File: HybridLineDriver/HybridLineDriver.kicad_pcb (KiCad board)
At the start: 2 copper layers, 100 x 100 mm, 34 parts, among them J1 XLR3, J2 Conn_01x03, J3 Conn_01x02, U1 OPA1679

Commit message: pcb cleanup
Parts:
- moved C6 2.67 mm to (113.0, 93.3), turned to -90 degrees
- moved C2 1.91 mm to (118.1, 101.6), turned to -90 degrees
- moved R18 1.80 mm to (128.3, 96.5)
- moved R3 1.53 mm to (109.2, 101.6), turned to 90 degrees
- moved R15 1.14 mm to (91.4, 100.3)
- moved R20 1.14 mm to (94.0, 100.3)
- moved R16 1.02 mm to (88.9, 97.4)
- moved R4 0.94 mm to (102.9, 116.2)
- moved R9 0.92 mm to (101.6, 120.0)
- moved C3 0.92 mm to (101.6, 122.6)
- moved R13 0.77 mm to (87.0, 106.3)
- moved C1 0.77 mm to (105.4, 109.2)
- moved RV1 0.76 mm to (97.5, 93.3)
- moved J3 0.64 mm to (134.6, 120.7), turned to 180 degrees
- moved R6 0.57 mm to (125.1, 99.7)
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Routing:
- net Net-(C2-Pad1): track 29.6 -> 34.5 mm
- net Net-(C2-Pad2): track 16.5 -> 20.3 mm
- net Net-(C6-Pad1): track 37.2 -> 40.3 mm
- net GND: track 14.3 -> 16.2 mm
- net Net-(R16-Pad2): track 8.49 -> 9.82 mm
- net Net-(U1B--): track 9.86 -> 11.0 mm
- net Net-(C6-Pad2): track 21.5 -> 22.6 mm
- net Net-(C5-Pad2): track 19.2 -> 20.2 mm
- net Net-(C3-Pad1): track 27.1 -> 28.1 mm
- net Net-(R7-Pad1): track 3.42 -> 4.29 mm
- net Net-(C4-Pad2): track 12.8 -> 11.9 mm
- net +15V: track 44.8 -> 44.0 mm
- net Net-(U1D--): track 14.6 -> 13.9 mm
- net Net-(U1C-+): track 10.6 -> 11.3 mm
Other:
- board size 100 x 100 mm -> 100 x 105 mm

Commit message: update pcb
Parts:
- moved RV1 4.38 mm to (93.3, 94.6)
- moved R3 4.02 mm to (108.0, 105.4)
- moved C3 3.42 mm to (100.3, 119.4), turned to 90 degrees
- moved C4 3.18 mm to (88.3, 106.7), turned to -90 degrees
- moved R4 2.62 mm to (105.4, 116.8)
- moved R9 1.42 mm to (102.9, 119.4), turned to 90 degrees
- moved R20 1.42 mm to (93.3, 101.6)
- moved R11 1.42 mm to (90.8, 123.2)
- moved R15 1.42 mm to (90.8, 101.6)
- moved R19 1.42 mm to (88.3, 123.2)
- moved R13 1.33 mm to (85.7, 106.7)
- moved R12 1.27 mm to (85.7, 113.7)
- moved R14 1.27 mm to (88.3, 116.8)
- moved R2 1.27 mm to (110.5, 105.4), turned to 90 degrees
- moved R16 1.20 mm to (88.3, 98.4)
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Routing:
- net Net-(C1-Pad2): track 15.4 -> 11.1 mm
- net Net-(C3-Pad1): track 28.1 -> 32.2 mm
- net Net-(U1D--): track 13.9 -> 17.8 mm
- net Net-(C4-Pad2): track 11.9 -> 8.02 mm
- net Net-(R16-Pad2): track 9.82 -> 6.05 mm
- net Net-(U1C--): track 12.7 -> 15.5 mm
- net Net-(U1B--): track 11.0 -> 8.93 mm
- net Net-(U1A--): track 8.17 -> 10.1 mm
- net Net-(C5-Pad2): track 20.2 -> 21.6 mm
- net Net-(U1A-+): track 6.64 -> 7.80 mm
- net Net-(R7-Pad1): track 4.29 -> 5.42 mm
- net Net-(C2-Pad1): track 34.5 -> 33.5 mm
- net Net-(U1D-+): track 11.6 -> 10.6 mm
- net GND: track 16.2 -> 15.5 mm
- net Net-(R2-Pad1): track 22.5 -> 21.9 mm

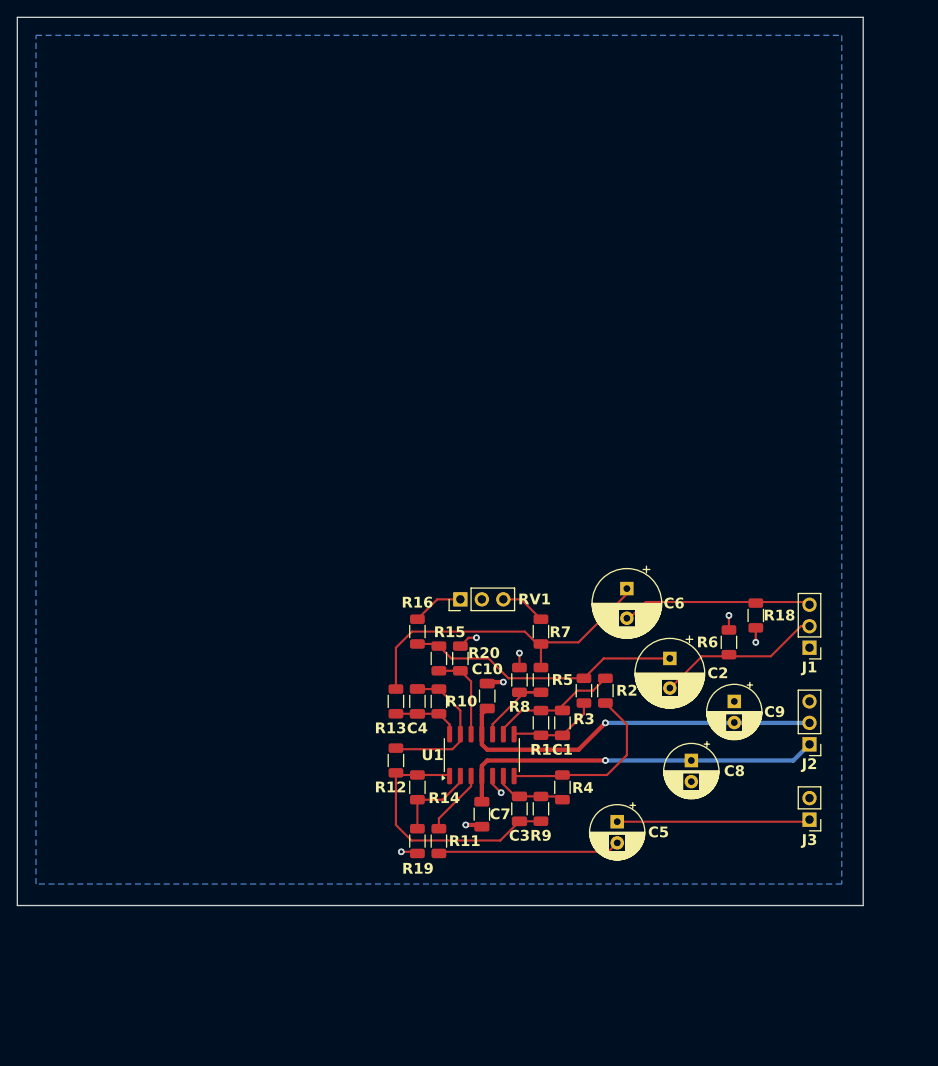
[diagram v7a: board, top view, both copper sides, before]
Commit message: added TLA Input
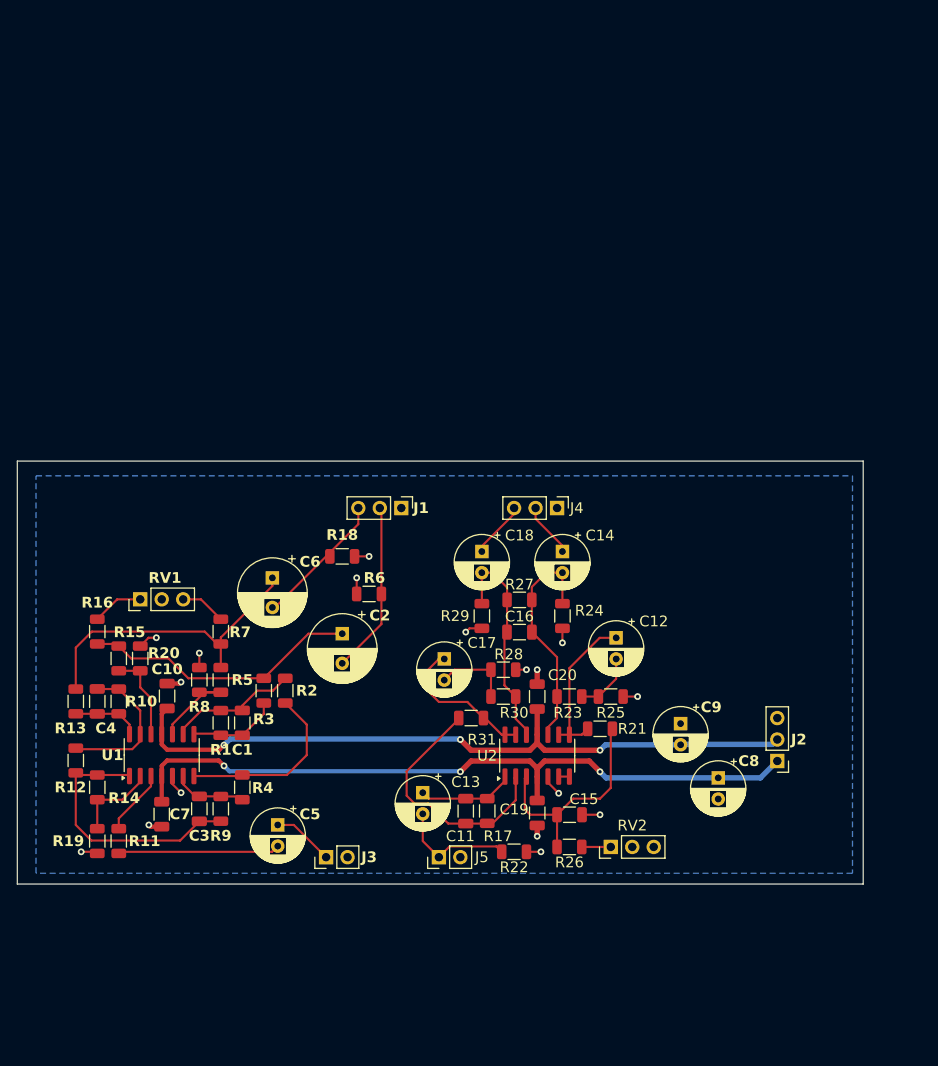
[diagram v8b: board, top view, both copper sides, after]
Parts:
- added C11: 22p, Capacitor_SMD:C_1206_3216Metric, F.Cu at (94.0, 119.6)
- added C12: 22u, Capacitor_THT:CP_Radial_D6.3mm_P2.50mm, F.Cu at (111.8, 99.2)
- added C13: 100u, Capacitor_THT:CP_Radial_D6.3mm_P2.50mm, F.Cu at (88.9, 117.5)
- added C14: 10u, Capacitor_THT:CP_Radial_D6.3mm_P2.50mm, F.Cu at (105.4, 89.0)
- added C15: 22p, Capacitor_SMD:C_1206_3216Metric, F.Cu at (106.2, 120.1)
- added C16: 220p, Capacitor_SMD:C_1206_3216Metric, F.Cu at (100.3, 98.5)
- added C17: 22u, Capacitor_THT:CP_Radial_D6.3mm_P2.50mm, F.Cu at (91.4, 101.7)
- added C18: 10u, Capacitor_THT:CP_Radial_D6.3mm_P2.50mm, F.Cu at (95.9, 89.0)
- added C19: 100n, Capacitor_SMD:C_1206_3216Metric, F.Cu at (102.4, 119.9)
- added C20: 100n, Capacitor_SMD:C_1206_3216Metric, F.Cu at (102.4, 106.1)
- added J4: XLR3, Connector_PinHeader_2.54mm:PinHeader_1x03_P2.54mm_Vertical, F.Cu at (104.8, 83.8)
- added J5: Conn_01x02, Connector_PinHeader_2.54mm:PinHeader_1x02_P2.54mm_Vertical, F.Cu at (90.8, 125.1)
- added R17: 2k, Resistor_SMD:R_1206_3216Metric, F.Cu at (96.5, 119.6)
- added R21: 2k7, Resistor_SMD:R_1206_3216Metric, F.Cu at (109.9, 109.9)
- added R22: 100k, Resistor_SMD:R_1206_3216Metric, F.Cu at (99.7, 124.5)
- added R23: 47k, Resistor_SMD:R_1206_3216Metric, F.Cu at (106.2, 106.1)
- added R24: 10M, Resistor_SMD:R_1206_3216Metric, F.Cu at (105.4, 96.6)
- added R25: 10k, Resistor_SMD:R_1206_3216Metric, F.Cu at (111.1, 106.1)
- added R26: 1k8, Resistor_SMD:R_1206_3216Metric, F.Cu at (106.2, 123.9)
- added R27: 22k, Resistor_SMD:R_1206_3216Metric, F.Cu at (100.3, 94.7)
- added R28: 10k, Resistor_SMD:R_1206_3216Metric, F.Cu at (98.4, 102.9)
- added R29: 10M, Resistor_SMD:R_1206_3216Metric, F.Cu at (95.9, 96.6)
- added R30: 47k, Resistor_SMD:R_1206_3216Metric, F.Cu at (98.4, 106.1)
- added R31: 2k7, Resistor_SMD:R_1206_3216Metric, F.Cu at (94.6, 108.6)
- added RV2: 500R, Connector_PinHeader_2.54mm:PinHeader_1x03_P2.54mm_Vertical, F.Cu at (111.1, 123.9)
- added U2: OPA1679, Package_SO:SOIC-14_3.9x8.7mm_P1.27mm, F.Cu at (102.4, 113.1)
- moved J3 57.3 mm to (77.5, 125.1), turned to 90 degrees
- moved J1 51.0 mm to (86.4, 83.8), turned to -90 degrees
- moved R18 49.4 mm to (79.4, 89.5), turned to 180 degrees
- moved R6 42.9 mm to (82.5, 94.0), turned to 0 degrees
- moved C6 41.9 mm to (71.1, 92.1)
- moved C5 40.1 mm to (71.8, 121.3)
- moved C2 38.8 mm to (79.4, 98.7)
- moved C1 37.8 mm to (67.6, 109.2)
- moved C4 37.8 mm to (50.4, 106.7)
- moved C7 37.8 mm to (58.0, 120.0)
- moved R1 37.8 mm to (65.0, 109.2)
- moved R10 37.8 mm to (53.0, 106.7)
- moved R11 37.8 mm to (53.0, 123.2)
- moved R14 37.8 mm to (50.4, 116.8)
- moved R15 37.8 mm to (53.0, 101.6)
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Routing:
- net +15V: track 44.0 -> 84.5 mm, vias 1 -> 3
- net -15V: track 44.9 -> 83.8 mm, vias 1 -> 3
- net Net-(U2A--): track 0.00 -> 30.6 mm
- net Net-(U2C-+): track 0.00 -> 27.1 mm
- net Net-(U2A-+): track 0.00 -> 26.6 mm
- net Net-(U2D-+): track 0.00 -> 26.0 mm
- net Net-(U2C--): track 0.00 -> 18.6 mm
- net Net-(U2D--): track 0.00 -> 17.9 mm
- net GND: track 15.5 -> 32.0 mm, vias 8 -> 17
- net Net-(J3-Pin_1): track 22.8 -> 7.29 mm
- net Net-(J5-Pin_1): track 0.00 -> 14.1 mm
- net Net-(C11-Pad1): track 0.00 -> 11.4 mm
- net Net-(C17-Pad2): track 0.00 -> 9.21 mm
- net Net-(C12-Pad2): track 0.00 -> 7.28 mm
- net Net-(C18-Pad1): track 0.00 -> 6.72 mm
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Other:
- board size 100 x 105 mm -> 100 x 50 mm
